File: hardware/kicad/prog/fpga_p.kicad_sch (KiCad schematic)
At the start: 33 parts, among them J3 PROG P, U10 iCE40HX4K-TQ144, U11 W25Q32JVSS, X1 25 MHz 3,3 V

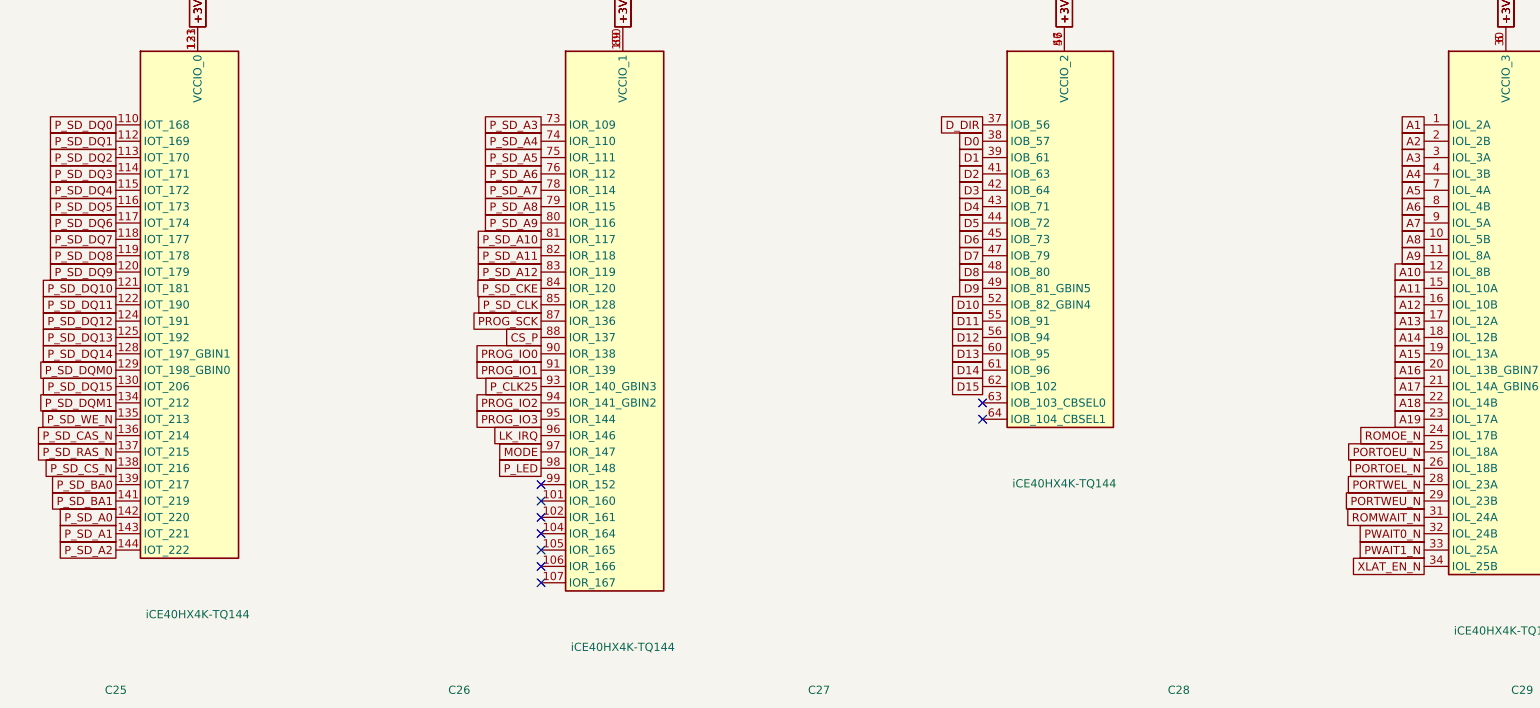
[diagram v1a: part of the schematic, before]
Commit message: Circuits imprimés 2 couches : placement et affectation des broches FPGA
- hardware/gen/pcb.py : empreintes et réseaux depuis boards.py, contour
  depuis outline.py ; ancres placées (contacts, rangée de tampons, FPGA,
  mémoires ; CHA : Pico au centre, microSD et bouton en haut), passifs
  au plus près de leur broche, masse coulée sur les deux faces.
- --pins : signaux des FPGA affectés aux broches tournées vers leur
  cible en conservant l'ordre circulaire (pins_opt.json, repris par
  fpga_pins.py) ; stable en trois passes.
- boards.py : canaux des tampons triés selon la position des contacts.
- hardware/gen/route.py : export Specctra, Freerouting, relecture de la
  session, DRC.
Placement-routage FPGA avec les nouvelles broches : en cours de
vérification.

Co-Authored-By: Claude Opus 5.5 <noreply@anthropic.com>
Claude-Session: https://claude.ai/code/session_01WKfXP1YJ8otGxZ5dsY6Agh
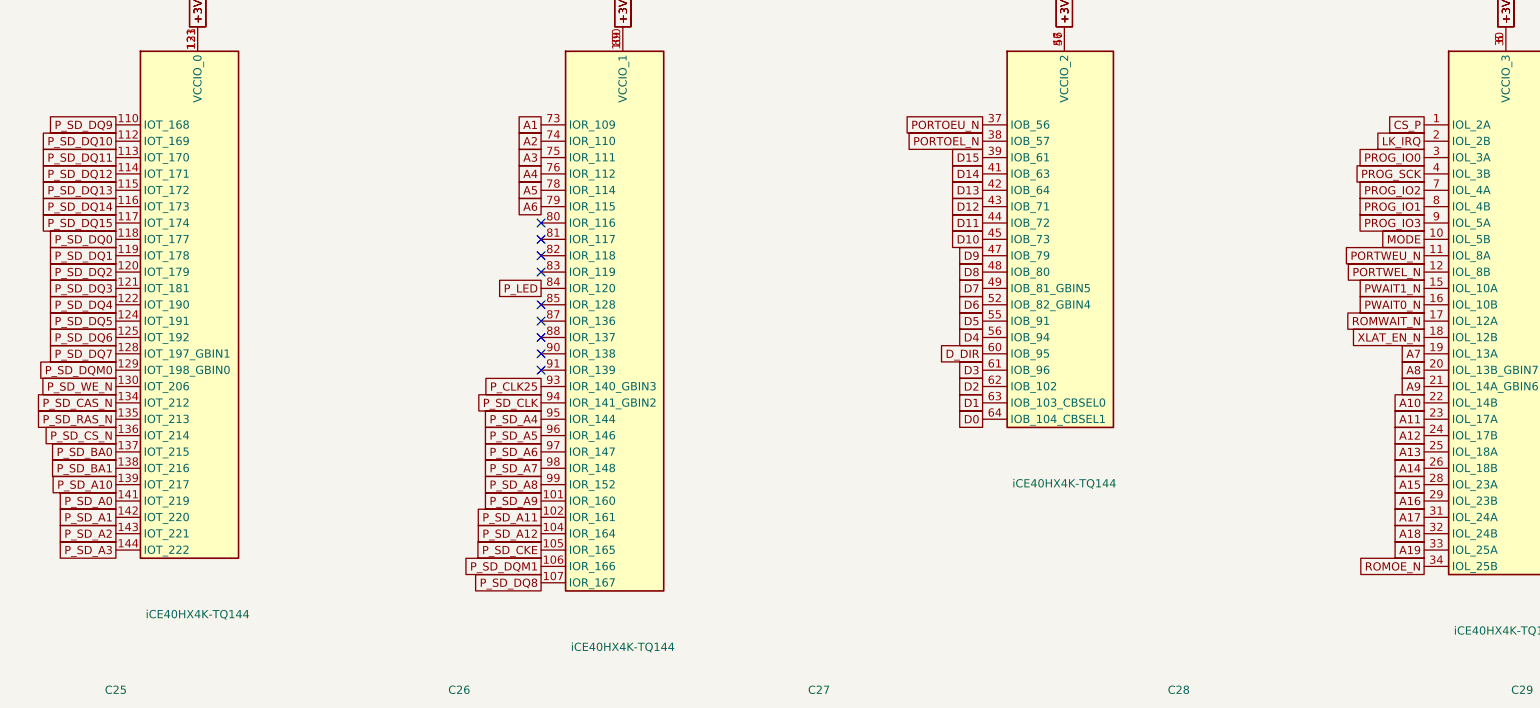
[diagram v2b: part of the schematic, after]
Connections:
- net A1: now also U10.73 (IOR_109); no longer U10.1 (IOL_2A)
- net A10: now also U10.22 (IOL_14B); no longer U10.12 (IOL_8B)
- net A11: now also U10.23 (IOL_17A); no longer U10.15 (IOL_10A)
- net A12: now also U10.24 (IOL_17B); no longer U10.16 (IOL_10B)
- net A13: now also U10.25 (IOL_18A); no longer U10.17 (IOL_12A)
- net A14: now also U10.26 (IOL_18B); no longer U10.18 (IOL_12B)
- net A15: now also U10.28 (IOL_23A); no longer U10.19 (IOL_13A)
- net A16: now also U10.29 (IOL_23B); no longer U10.20 (IOL_13B_GBIN7)
- net A17: now also U10.31 (IOL_24A); no longer U10.21 (IOL_14A_GBIN6)
- net A18: now also U10.32 (IOL_24B); no longer U10.22 (IOL_14B)
- net A19: now also U10.33 (IOL_25A); no longer U10.23 (IOL_17A)
- net A2: now also U10.74 (IOR_110); no longer U10.2 (IOL_2B)
- net A3: now also U10.75 (IOR_111); no longer U10.3 (IOL_3A)
- net A4: now also U10.76 (IOR_112); no longer U10.4 (IOL_3B)
- net A5: now also U10.78 (IOR_114); no longer U10.7 (IOL_4A)
- net A6: now also U10.79 (IOR_115); no longer U10.8 (IOL_4B)
- net A7: now also U10.19 (IOL_13A); no longer U10.9 (IOL_5A)
- net A8: now also U10.20 (IOL_13B_GBIN7); no longer U10.10 (IOL_5B)
- net A9: now also U10.21 (IOL_14A_GBIN6); no longer U10.11 (IOL_8A)
- net CS_P: now also U10.1 (IOL_2A); no longer U10.88 (IOR_137)
- net D0: now also U10.64 (IOB_104_CBSEL1); no longer U10.38 (IOB_57)
- net D1: now also U10.63 (IOB_103_CBSEL0); no longer U10.39 (IOB_61)
- net D10: now also U10.45 (IOB_73); no longer U10.52 (IOB_82_GBIN4)
- net D11: now also U10.44 (IOB_72); no longer U10.55 (IOB_91)
- net D12: now also U10.43 (IOB_71); no longer U10.56 (IOB_94)
- net D13: now also U10.42 (IOB_64); no longer U10.60 (IOB_95)
- net D14: now also U10.41 (IOB_63); no longer U10.61 (IOB_96)
- net D15: now also U10.39 (IOB_61); no longer U10.62 (IOB_102)
- net D2: now also U10.62 (IOB_102); no longer U10.41 (IOB_63)
- net D3: now also U10.61 (IOB_96); no longer U10.42 (IOB_64)
- net D4: now also U10.56 (IOB_94); no longer U10.43 (IOB_71)
- net D5: now also U10.55 (IOB_91); no longer U10.44 (IOB_72)
- net D6: now also U10.52 (IOB_82_GBIN4); no longer U10.45 (IOB_73)
- net D7: now also U10.49 (IOB_81_GBIN5); no longer U10.47 (IOB_79)
- net D9: now also U10.47 (IOB_79); no longer U10.49 (IOB_81_GBIN5)
- net D_DIR: now also U10.60 (IOB_95); no longer U10.37 (IOB_56)
- net LK_IRQ: now also U10.2 (IOL_2B); no longer U10.96 (IOR_146)
- net MODE: now also U10.10 (IOL_5B); no longer U10.97 (IOR_147)
- net PORTOEL_N: now also U10.38 (IOB_57); no longer U10.26 (IOL_18B)
- net PORTOEU_N: now also U10.37 (IOB_56); no longer U10.25 (IOL_18A)
- net PORTWEL_N: now also U10.12 (IOL_8B); no longer U10.28 (IOL_23A)
- net PORTWEU_N: now also U10.11 (IOL_8A); no longer U10.29 (IOL_23B)
- net PROG_IO0: now also U10.3 (IOL_3A); no longer U10.90 (IOR_138)
- net PROG_IO1: now also U10.8 (IOL_4B); no longer U10.91 (IOR_139)
- net PROG_IO2: now also U10.7 (IOL_4A); no longer U10.94 (IOR_141_GBIN2)
- net PROG_IO3: now also U10.9 (IOL_5A); no longer U10.95 (IOR_144)
- net PROG_SCK: now also U10.4 (IOL_3B); no longer U10.87 (IOR_136)
- net PWAIT0_N: now also U10.16 (IOL_10B); no longer U10.32 (IOL_24B)
- net PWAIT1_N: now also U10.15 (IOL_10A); no longer U10.33 (IOL_25A)
- net P_LED: now also U10.84 (IOR_120); no longer U10.98 (IOR_148)
- net P_SD_A0: now also U10.141 (IOT_219); no longer U10.142 (IOT_220)
- net P_SD_A1: now also U10.142 (IOT_220); no longer U10.143 (IOT_221)
- net P_SD_A10: now also U10.139 (IOT_217); no longer U10.81 (IOR_117)
- net P_SD_A11: now also U10.102 (IOR_161); no longer U10.82 (IOR_118)
- net P_SD_A12: now also U10.104 (IOR_164); no longer U10.83 (IOR_119)
- net P_SD_A2: now also U10.143 (IOT_221); no longer U10.144 (IOT_222)
- net P_SD_A3: now also U10.144 (IOT_222); no longer U10.73 (IOR_109)
- net P_SD_A4: now also U10.95 (IOR_144); no longer U10.74 (IOR_110)
- net P_SD_A5: now also U10.96 (IOR_146); no longer U10.75 (IOR_111)
- net P_SD_A6: now also U10.97 (IOR_147); no longer U10.76 (IOR_112)
- net P_SD_A7: now also U10.98 (IOR_148); no longer U10.78 (IOR_114)
- net P_SD_A8: now also U10.99 (IOR_152); no longer U10.79 (IOR_115)
- net P_SD_A9: now also U10.101 (IOR_160); no longer U10.80 (IOR_116)
- net P_SD_BA0: now also U10.137 (IOT_215); no longer U10.139 (IOT_217)
- net P_SD_BA1: now also U10.138 (IOT_216); no longer U10.141 (IOT_219)
- net P_SD_CAS_N: now also U10.134 (IOT_212); no longer U10.136 (IOT_214)
- net P_SD_CKE: now also U10.105 (IOR_165); no longer U10.84 (IOR_120)
- net P_SD_CLK: now also U10.94 (IOR_141_GBIN2); no longer U10.85 (IOR_128)
- net P_SD_CS_N: now also U10.136 (IOT_214); no longer U10.138 (IOT_216)
- net P_SD_DQ0: now also U10.118 (IOT_177); no longer U10.110 (IOT_168)
- net P_SD_DQ1: now also U10.119 (IOT_178); no longer U10.112 (IOT_169)
- net P_SD_DQ10: now also U10.112 (IOT_169); no longer U10.121 (IOT_181)
- net P_SD_DQ11: now also U10.113 (IOT_170); no longer U10.122 (IOT_190)
- net P_SD_DQ12: now also U10.114 (IOT_171); no longer U10.124 (IOT_191)
- net P_SD_DQ13: now also U10.115 (IOT_172); no longer U10.125 (IOT_192)
- net P_SD_DQ14: now also U10.116 (IOT_173); no longer U10.128 (IOT_197_GBIN1)
- net P_SD_DQ15: now also U10.117 (IOT_174); no longer U10.130 (IOT_206)
- net P_SD_DQ2: now also U10.120 (IOT_179); no longer U10.113 (IOT_170)
- net P_SD_DQ3: now also U10.121 (IOT_181); no longer U10.114 (IOT_171)
- net P_SD_DQ4: now also U10.122 (IOT_190); no longer U10.115 (IOT_172)
- net P_SD_DQ5: now also U10.124 (IOT_191); no longer U10.116 (IOT_173)
- net P_SD_DQ6: now also U10.125 (IOT_192); no longer U10.117 (IOT_174)
- net P_SD_DQ7: now also U10.128 (IOT_197_GBIN1); no longer U10.118 (IOT_177)
- net P_SD_DQ8: now also U10.107 (IOR_167); no longer U10.119 (IOT_178)
- net P_SD_DQ9: now also U10.110 (IOT_168); no longer U10.120 (IOT_179)
- net P_SD_DQM1: now also U10.106 (IOR_166); no longer U10.134 (IOT_212)
- net P_SD_RAS_N: now also U10.135 (IOT_213); no longer U10.137 (IOT_215)
- net P_SD_WE_N: now also U10.130 (IOT_206); no longer U10.135 (IOT_213)
- net ROMOE_N: now also U10.34 (IOL_25B); no longer U10.24 (IOL_17B)
- net ROMWAIT_N: now also U10.17 (IOL_12A); no longer U10.31 (IOL_24A)
- net XLAT_EN_N: now also U10.18 (IOL_12B); no longer U10.34 (IOL_25B)

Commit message: FPGA configurés par le RP2350 depuis la carte SD (plus de flash)
- Matériel : flash SPI retirées (4 W25Q32, 12 résistances, 4
  condensateurs). Le bus de liaison arrive sur les broches de
  configuration des iCE40 (LK_SCK -> 70 SCK, LK_IO[0] -> 68 SDI,
  LK_CS_N -> 71 SS), qui redeviennent ces entrées après le démarrage.
  CRESET_N commun aux 4 FPGA, tiré à la masse, piloté par le RP2350
  (GP28) ; câble PROG-CHA en 2 x 7 (CRESET_N + masse). Connecteur 2 x 3
  de secours par FPGA (iceprog -S).
- Firmware : fpga_boot.c (reset commun en mode SPI esclave, envoi des
  SDAES/fpga_*.bin l'un après l'autre, contrôle de CDONE) ; testé sur
  PC (bitstreams reçus à l'identique, FPGA laissés en reset si un
  fichier manque).
- make -C hdl sd : fichiers à copier sur la carte SD.
- PCB : table de placement et références des FPGA mises à jour,
  broches réoptimisées.
Placement-routage des FPGA avec les nouvelles broches : en cours.

Co-Authored-By: Claude Opus 5.5 <noreply@anthropic.com>
Claude-Session: https://claude.ai/code/session_01WKfXP1YJ8otGxZ5dsY6Agh
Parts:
- removed C39: 100n, Capacitor_SMD:C_0603_1608Metric, symbol Device:C
- removed R14, R15: 10k, Resistor_SMD:R_0603_1608Metric, symbol Device:R
- removed R16: 470, Resistor_SMD:R_0603_1608Metric, symbol Device:R
- removed U11: W25Q32JVSS, Package_SO:SOIC-8_5.23x5.23mm_P1.27mm, symbol Memory_Flash:W25Q32JVSS
- J3: value PROG P -> CONF P
- R13: value 10k -> 470
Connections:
- net P_FL_DO is gone; now on net PROG_IO0: J3.4 (Pin_4), U10.68 (IOB_106_SDI)
- net P_FL_SCK is gone; now on net PROG_SCK: J3.1 (Pin_1), U10.70 (IOB_107_SCK)
- net +3V3: no longer R12.1, R13.1
- net A1: now also U10.74 (IOR_110); no longer U10.73 (IOR_109)
- net A10: now also U10.23 (IOL_17A); no longer U10.22 (IOL_14B)
- net A11: now also U10.24 (IOL_17B); no longer U10.23 (IOL_17A)
- net A12: now also U10.25 (IOL_18A); no longer U10.24 (IOL_17B)
- net A13: now also U10.26 (IOL_18B); no longer U10.25 (IOL_18A)
- net A14: now also U10.28 (IOL_23A); no longer U10.26 (IOL_18B)
- net A15: now also U10.29 (IOL_23B); no longer U10.28 (IOL_23A)
- net A16: now also U10.31 (IOL_24A); no longer U10.29 (IOL_23B)
- net A17: now also U10.32 (IOL_24B); no longer U10.31 (IOL_24A)
- net A18: now also U10.33 (IOL_25A); no longer U10.32 (IOL_24B)
- net A19: now also U10.34 (IOL_25B); no longer U10.33 (IOL_25A)
- net A2: now also U10.75 (IOR_111); no longer U10.74 (IOR_110)
- net A3: now also U10.76 (IOR_112); no longer U10.75 (IOR_111)
- net A4: now also U10.78 (IOR_114); no longer U10.76 (IOR_112)
- net A5: now also U10.79 (IOR_115); no longer U10.78 (IOR_114)
- net A6: now also U10.80 (IOR_116); no longer U10.79 (IOR_115)
- net A7: now also U10.20 (IOL_13B_GBIN7); no longer U10.19 (IOL_13A)
- net A8: now also U10.21 (IOL_14A_GBIN6); no longer U10.20 (IOL_13B_GBIN7)
- net A9: now also U10.22 (IOL_14B); no longer U10.21 (IOL_14A_GBIN6)
- net CS_P: now also J3.2 (Pin_2), U10.71 (IOB_108_SS); no longer U10.1 (IOL_2A)
- net D0: now also U10.73 (IOR_109); no longer U10.64 (IOB_104_CBSEL1)
- net D1: now also U10.64 (IOB_104_CBSEL1); no longer U10.63 (IOB_103_CBSEL0)
- net D10: now also U10.47 (IOB_79); no longer U10.45 (IOB_73)
- net D11: now also U10.45 (IOB_73); no longer U10.44 (IOB_72)
- net D12: now also U10.44 (IOB_72); no longer U10.43 (IOB_71)
- net D13: now also U10.43 (IOB_71); no longer U10.42 (IOB_64)
- net D14: now also U10.42 (IOB_64); no longer U10.41 (IOB_63)
- net D15: now also U10.41 (IOB_63); no longer U10.39 (IOB_61)
- net D2: now also U10.63 (IOB_103_CBSEL0); no longer U10.62 (IOB_102)
- net D3: now also U10.62 (IOB_102); no longer U10.61 (IOB_96)
- net D4: now also U10.60 (IOB_95); no longer U10.56 (IOB_94)
- net D5: now also U10.56 (IOB_94); no longer U10.55 (IOB_91)
- net D6: now also U10.55 (IOB_91); no longer U10.52 (IOB_82_GBIN4)
- net D7: now also U10.52 (IOB_82_GBIN4); no longer U10.49 (IOB_81_GBIN5)
- net D8: now also U10.49 (IOB_81_GBIN5); no longer U10.48 (IOB_80)
- net D9: now also U10.48 (IOB_80); no longer U10.47 (IOB_79)
- net D_DIR: now also U10.61 (IOB_96); no longer U10.60 (IOB_95)
- net GND: now also R12.2
- net LK_IRQ: now also U10.7 (IOL_4A); no longer U10.2 (IOL_2B)
- net MODE: now also U10.11 (IOL_8A); no longer U10.10 (IOL_5B)
- net PORTOEL_N: now also U10.39 (IOB_61); no longer U10.38 (IOB_57)
- net PORTOEU_N: now also U10.38 (IOB_57); no longer U10.37 (IOB_56)
- net PORTWEL_N: now also U10.15 (IOL_10A); no longer U10.12 (IOL_8B)
- net PORTWEU_N: now also U10.12 (IOL_8B); no longer U10.11 (IOL_8A)
- net PROG_IO0: no longer U10.3 (IOL_3A)
- net PROG_IO1: now also U10.9 (IOL_5A); no longer U10.8 (IOL_4B)
- net PROG_IO2: now also U10.8 (IOL_4B); no longer U10.7 (IOL_4A)
- net PROG_IO3: now also U10.10 (IOL_5B); no longer U10.9 (IOL_5A)
- net PROG_SCK: no longer U10.4 (IOL_3B)
- net PWAIT0_N: now also U10.17 (IOL_12A); no longer U10.16 (IOL_10B)
- net PWAIT1_N: now also U10.16 (IOL_10B); no longer U10.15 (IOL_10A)
- net P_LED: now also R13.1, U10.87 (IOR_136); no longer U10.84 (IOR_120)
- net P_LED_K: now also R13.2
- net P_SD_A0: now also U10.1 (IOL_2A); no longer U10.141 (IOT_219)
- net P_SD_A1: now also U10.2 (IOL_2B); no longer U10.142 (IOT_220)
- net P_SD_A10: now also U10.144 (IOT_222); no longer U10.139 (IOT_217)
- net P_SD_A11: now also U10.106 (IOR_166); no longer U10.102 (IOR_161)
- net P_SD_A12: now also U10.107 (IOR_167); no longer U10.104 (IOR_164)
- net P_SD_A2: now also U10.3 (IOL_3A); no longer U10.143 (IOT_221)
- net P_SD_A3: now also U10.4 (IOL_3B); no longer U10.144 (IOT_222)
- net P_SD_A4: now also U10.98 (IOR_148); no longer U10.95 (IOR_144)
- net P_SD_A5: now also U10.99 (IOR_152); no longer U10.96 (IOR_146)
- net P_SD_A6: now also U10.101 (IOR_160); no longer U10.97 (IOR_147)
- net P_SD_A7: now also U10.102 (IOR_161); no longer U10.98 (IOR_148)
- net P_SD_A8: now also U10.104 (IOR_164); no longer U10.99 (IOR_152)
- net P_SD_A9: now also U10.105 (IOR_165); no longer U10.101 (IOR_160)
- net P_SD_BA0: now also U10.142 (IOT_220); no longer U10.137 (IOT_215)
- net P_SD_BA1: now also U10.143 (IOT_221); no longer U10.138 (IOT_216)
- net P_SD_CAS_N: now also U10.138 (IOT_216); no longer U10.134 (IOT_212)
- net P_SD_CKE: now also U10.110 (IOT_168); no longer U10.105 (IOR_165)
- net P_SD_CLK: now also U10.97 (IOR_147); no longer U10.94 (IOR_141_GBIN2)
- net P_SD_CS_N: now also U10.141 (IOT_219); no longer U10.136 (IOT_214)
- net P_SD_DQ0: now also U10.121 (IOT_181); no longer U10.118 (IOT_177)
- net P_SD_DQ1: now also U10.122 (IOT_190); no longer U10.119 (IOT_178)
- net P_SD_DQ10: now also U10.115 (IOT_172); no longer U10.112 (IOT_169)
- net P_SD_DQ11: now also U10.116 (IOT_173); no longer U10.113 (IOT_170)
- net P_SD_DQ12: now also U10.117 (IOT_174); no longer U10.114 (IOT_171)
- net P_SD_DQ13: now also U10.118 (IOT_177); no longer U10.115 (IOT_172)
- net P_SD_DQ14: now also U10.119 (IOT_178); no longer U10.116 (IOT_173)
- net P_SD_DQ15: now also U10.120 (IOT_179); no longer U10.117 (IOT_174)
- net P_SD_DQ2: now also U10.124 (IOT_191); no longer U10.120 (IOT_179)
- net P_SD_DQ3: now also U10.125 (IOT_192); no longer U10.121 (IOT_181)
- net P_SD_DQ4: now also U10.128 (IOT_197_GBIN1); no longer U10.122 (IOT_190)
- net P_SD_DQ5: now also U10.130 (IOT_206); no longer U10.124 (IOT_191)
- net P_SD_DQ6: now also U10.134 (IOT_212); no longer U10.125 (IOT_192)
- net P_SD_DQ7: now also U10.135 (IOT_213); no longer U10.128 (IOT_197_GBIN1)
- net P_SD_DQ8: now also U10.113 (IOT_170); no longer U10.107 (IOR_167)
- net P_SD_DQ9: now also U10.114 (IOT_171); no longer U10.110 (IOT_168)
- net P_SD_DQM0: now also U10.136 (IOT_214); no longer U10.129 (IOT_198_GBIN0)
- net P_SD_DQM1: now also U10.112 (IOT_169); no longer U10.106 (IOR_166)
- net P_SD_RAS_N: now also U10.139 (IOT_217); no longer U10.135 (IOT_213)
- net P_SD_WE_N: now also U10.137 (IOT_215); no longer U10.130 (IOT_206)
- net ROMOE_N: now also U10.37 (IOB_56); no longer U10.34 (IOL_25B)
- net ROMWAIT_N: now also U10.18 (IOL_12B); no longer U10.17 (IOL_12A)
- net XLAT_EN_N: now also U10.19 (IOL_13A); no longer U10.18 (IOL_12B)
- net P_CRESET_N renamed CRESET_N
- net CRESET_N: now also R12.1; no longer R12.2
- removed net P_FL_CS_N: J3.2 (Pin_2), R13.2, U10.71 (IOB_108_SS)
- net P_FL_DI renamed P_SDO
- no-connect marks 17 -> 20
